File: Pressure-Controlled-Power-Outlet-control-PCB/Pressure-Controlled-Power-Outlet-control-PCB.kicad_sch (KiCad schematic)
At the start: 25 parts, among them J1 Analog water pressure sensor 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, J2 1017514, K1 T9GV5L24-24, K2 T9GV5L24-24, Q1 2N3906, Q2 IRF540N, Q3 IRF540N, Q4 2N3906, U1 Pico, U2 LM324, U3 LF50_TO220

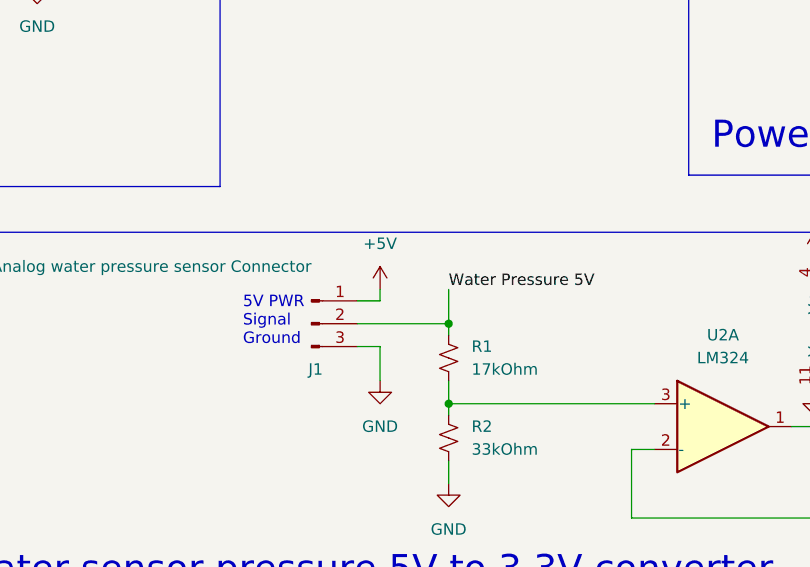
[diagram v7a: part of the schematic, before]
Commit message: updated to use the sen0257 WPS
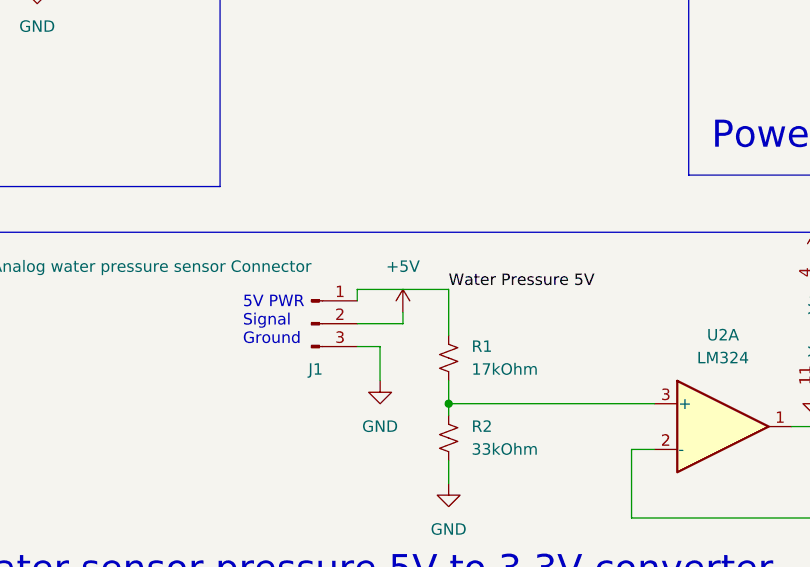
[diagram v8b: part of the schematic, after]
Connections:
- net +5V: now also J1.2 (Pin_2); no longer J1.1 (Pin_1)
- net Water Pressure 5V: now also J1.1 (Pin_1); no longer J1.2 (Pin_2)
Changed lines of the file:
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@@
     (title "Pressure Controlled Power Outlet")
     (date "2024-07-18")
-    (rev "V1.0")
+    (rev "V1.1.1")
   )
   (junction (at 121.92 175.26) (diameter 0) (color 0 0 0 0)
@@
   )
   (junction (at 162.56 33.02) (diameter 0) (color 0 0 0 0)
-  )
-  (junction (at 121.92 166.37) (diameter 0) (color 0 0 0 0)
   )
   (junction (at 91.44 27.94) (diameter 0) (color 0 0 0 0)
@@
     (stroke (width 0) (type default))
   )
+  (wire (pts (xy 111.76 162.56) (xy 111.76 163.83))
+    (stroke (width 0) (type default))
+  )
   (wire (pts (xy 190.5 125.73) (xy 190.5 124.46))
     (stroke (width 0) (type default))
   )
+  (wire (pts (xy 116.84 166.37) (xy 116.84 165.1))
+    (stroke (width 0) (type default))
+  )
   (wire (pts (xy 175.26 43.18) (xy 175.26 40.64))
     (stroke (width 0) (type default))
@@
     (stroke (width 0) (type default))
   )
+  (wire (pts (xy 121.92 162.56) (xy 121.92 167.64))
+    (stroke (width 0) (type default))
+  )
   (wire (pts (xy 189.23 33.02) (xy 182.88 33.02))
     (stroke (width 0) (type default))
@@
     (stroke (width 0) (type default))
   )
-  (wire (pts (xy 121.92 166.37) (xy 111.76 166.37))
-    (stroke (width 0) (type default))
-  )
   (wire (pts (xy 71.12 27.94) (xy 91.44 27.94))
     (stroke (width 0) (type default))
@@
     (stroke (width 0) (type default))
   )
-  (wire (pts (xy 114.3 163.83) (xy 111.76 163.83))
-    (stroke (width 0) (type default))
-  )
   (wire (pts (xy 142.24 180.34) (xy 144.78 180.34))
     (stroke (width 0) (type default))
@@
     (stroke (width 0) (type default))
   )
+  (wire (pts (xy 111.76 162.56) (xy 121.92 162.56))
+    (stroke (width 0) (type default))
+  )
   (wire (pts (xy 91.44 26.67) (xy 91.44 27.94))
     (stroke (width 0) (type default))
   )
-  (wire (pts (xy 121.92 167.64) (xy 121.92 166.37))
-    (stroke (width 0) (type default))
-  )
   (wire (pts (xy 91.44 41.91) (xy 91.44 48.26))
     (stroke (width 0) (type default))
@@
     (stroke (width 0) (type default))
   )
-  (wire (pts (xy 121.92 162.56) (xy 121.92 166.37))
-    (stroke (width 0) (type default))
-  )
   (wire (pts (xy 201.93 138.43) (xy 224.79 138.43))
     (stroke (width 0) (type default))
   )
-  (wire (pts (xy 114.3 162.56) (xy 114.3 163.83))
-    (stroke (width 0) (type default))
-  )
   (wire (pts (xy 224.79 130.81) (xy 224.79 138.43))
     (stroke (width 0) (type default))
@@
   )
   (wire (pts (xy 121.92 181.61) (xy 121.92 184.15))
+    (stroke (width 0) (type default))
+  )
+  (wire (pts (xy 111.76 166.37) (xy 116.84 166.37))
     (stroke (width 0) (type default))
   )
@@
     )
   )
-  (symbol (lib_id "power:+5V") (at 114.3 162.56 0) (unit 1)
-    (in_bom yes) (on_board yes) (dnp no) (fields_autoplaced)
-    (property "Reference" "#PWR01" (at 114.3 166.37 0)
-      (effects (font (size 1.27 1.27)) hide)
-    )
-    (property "Value" "+5V" (at 114.3 157.48 0)
-      (effects (font (size 1.27 1.27)))
-    )
-    (property "Footprint" "" (at 114.3 162.56 0)
-      (effects (font (size 1.27 1.27)) hide)
-    )
-    (property "Datasheet" "" (at 114.3 162.56 0)
-      (effects (font (size 1.27 1.27)) hide)
-    )
-    (pin "1")
-    (instances
-      (project "Pressure-Controlled-Power-Outlet-control-PCB"
-        (path "/db34d92e-5e84-4492-8b7e-15d9a09f9218"
-          (reference "#PWR01") (unit 1)
-        )
-      )
-    )
-  )
   (symbol (lib_id "Amplifier_Operational:LM324") (at 152.4 177.8 0) (unit 1)
     (in_bom yes) (on_board yes) (dnp no) (fields_autoplaced)
@@
         )
       )
+    )
+  )
+  (symbol (lib_id "power:+5V") (at 116.84 165.1 0) (unit 1)
+    (in_bom yes) (on_board yes) (dnp no) (fields_autoplaced)
+    (property "Reference" "#PWR01" (at 116.84 168.91 0)
+      (effects (font (size 1.27 1.27)) hide)
+    )
+    (property "Value" "+5V" (at 116.84 160.02 0)
+      (effects (font (size 1.27 1.27)))
+    )
+    (property "Footprint" "" (at 116.84 165.1 0)
+      (effects (font (size 1.27 1.27)) hide)
+    )
+    (property "Datasheet" "" (at 116.84 165.1 0)
+      (effects (font (size 1.27 1.27)) hide)
+    )
+    (pin "1")
+    (instances
+      (project "Pressure-Controlled-Power-Outlet-control-PCB"
+        (path "/db34d92e-5e84-4492-8b7e-15d9a09f9218"
+          (reference "#PWR01") (unit 1)
+        )
+      )
